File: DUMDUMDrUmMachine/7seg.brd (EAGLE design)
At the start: 100 x 80 mm, 11 parts

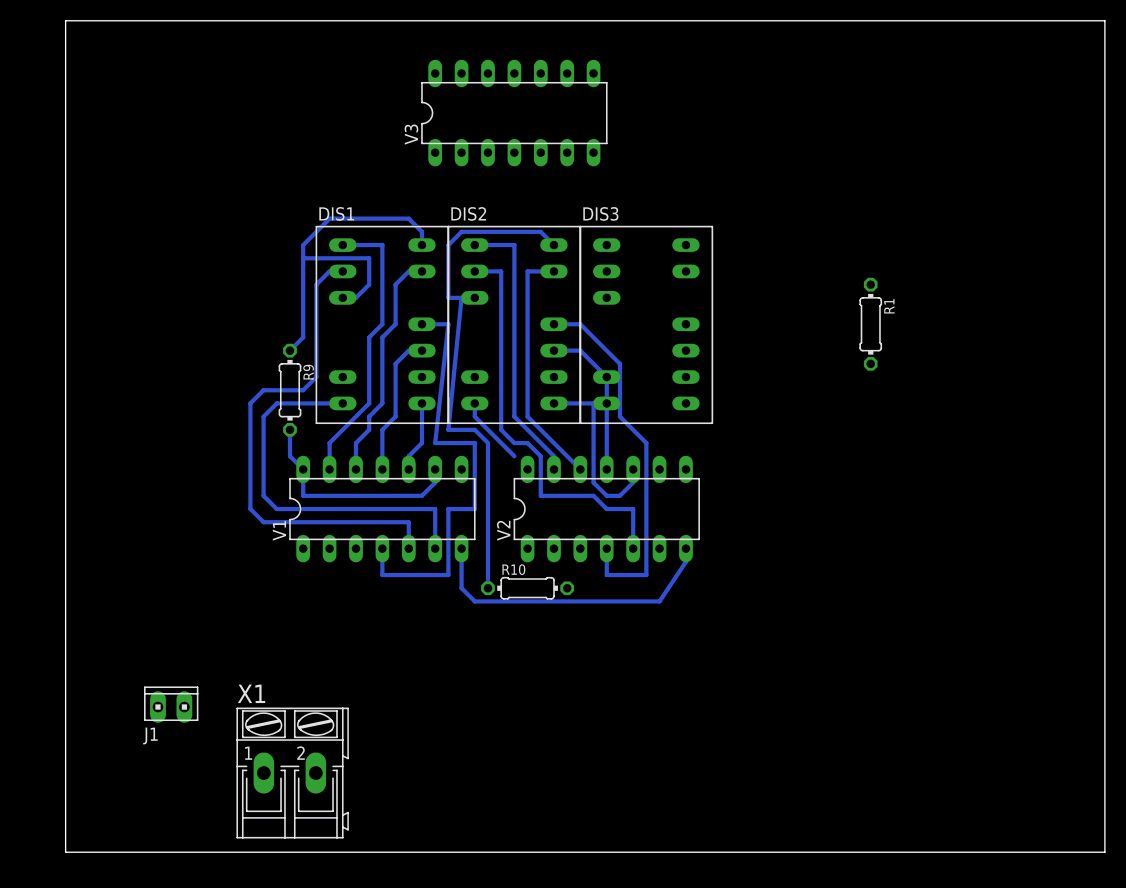
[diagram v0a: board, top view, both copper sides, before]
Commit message: 7seg-pcb should be finnished, also changed text in power-pcb
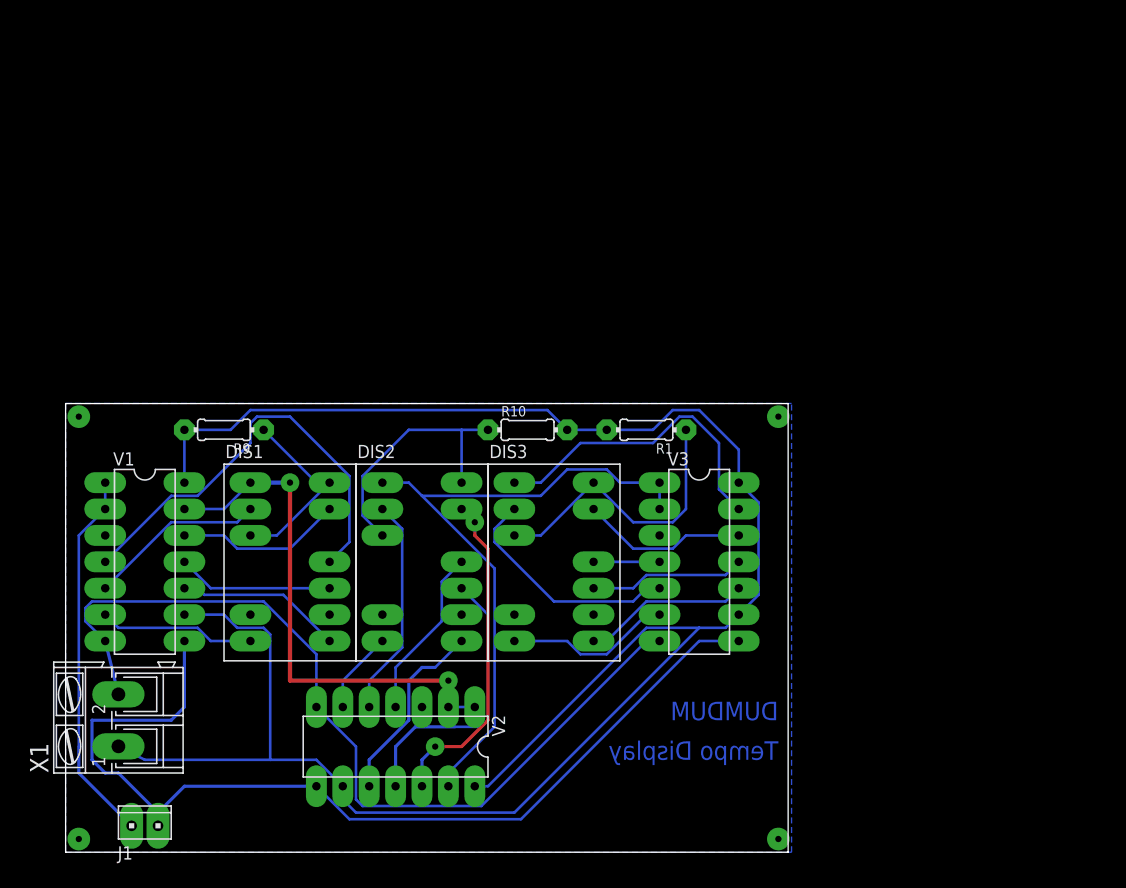
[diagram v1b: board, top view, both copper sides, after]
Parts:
- moved V3 46.7 mm to (61.0, 27.9), turned to 270 degrees
- moved V2 30.6 mm to (31.8, 10.2), turned to 180 degrees
- moved DIS1 24.5 mm to (21.6, 27.9)
- moved DIS2 24.5 mm to (34.3, 27.9)
- moved DIS3 24.5 mm to (47.0, 27.9)
- moved R1 23.9 mm to (55.9, 40.6), turned to 180 degrees
- moved V1 23.4 mm to (7.62, 27.9), turned to 270 degrees
- moved X1 17.3 mm to (5.08, 12.7), turned to 90 degrees
- moved R10 15.2 mm to (44.5, 40.6)
- moved J1 11.7 mm to (7.62, 2.54)
- moved R9 7.41 mm to (15.2, 40.6), turned to 180 degrees
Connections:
- removed net +UB: V3.14
- removed net -UB: V3.7
- net +5V: now also V3.14
- net GND: now also V3.7
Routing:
- net +5V: track 21.4 -> 199.6 mm
- net CLOCK_PIN_164: track 0.00 -> 94.6 mm
- net GND: track 29.2 -> 85.4 mm
- net N$1: track 27.0 -> 64.0 mm
- net DATA_PIN_164: track 0.00 -> 36.2 mm
- net N$3: track 47.8 -> 17.1 mm
- net N$22: track 0.00 -> 30.5 mm
- net N$24: track 0.00 -> 28.3 mm
- net N$23: track 49.9 -> 25.5 mm
- net N$9: track 27.5 -> 50.6 mm, vias 0 -> 2
- net N$17: track 0.00 -> 22.7 mm
- net N$4: track 36.6 -> 15.0 mm
- net N$16: track 36.9 -> 17.8 mm
- net N$10: track 35.7 -> 16.6 mm
- net N$11: track 39.7 -> 21.2 mm
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- added copper zone on layer 16, net N$29
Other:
- board size 100 x 80 mm -> 69.5 x 43.2 mm
- board text added: "DUMDUM"
- board text added: "Tempo Display"
